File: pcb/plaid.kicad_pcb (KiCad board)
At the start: 2 copper layers, 228 x 98 mm, 134 parts, among them J2 AVR_ISP_6, J3 Conn_01x04, SW1 SW_Push, SW10 SW_Push, SW11 SW_Push, SW12 SW_Push, SW13 SW_Push, SW14 SW_Push, SW15 SW_Push, SW16 SW_Push, SW17 SW_Push, SW18 SW_Push, SW19 SW_Push, SW2 SW_Push, SW20 SW_Push, SW21 SW_Push, SW22 SW_Push, SW23 SW_Push, SW24 SW_Push, SW25 SW_Push, SW26 SW_Push, SW27 SW_Push, SW28 SW_Push, SW29 SW_Push, SW3 SW_Push, SW30 SW_Push, SW31 SW_Push, SW32 SW_Push, SW33 SW_Push, SW34 SW_Push, SW35 SW_Push, SW36 SW_Push, SW37 SW_Push, SW38 SW_Push, SW39 SW_Push, SW4 SW_Push, SW40 SW_Push, SW41 SW_Push, SW42 SW_Push, SW43 SW_Push, SW44 SW_Push, SW45 SW_Push, SW46 SW_Push, SW47 SW_Push, SW48 SW_Push, SW49 SW_Push, SW5 SW_Push, SW50 RESET, SW51 BOOT, SW6 SW_Push, SW7 SW_Push, SW8 SW_Push, SW9 SW_Push, U1 ATMEGA328-PU, Y1 16MHz

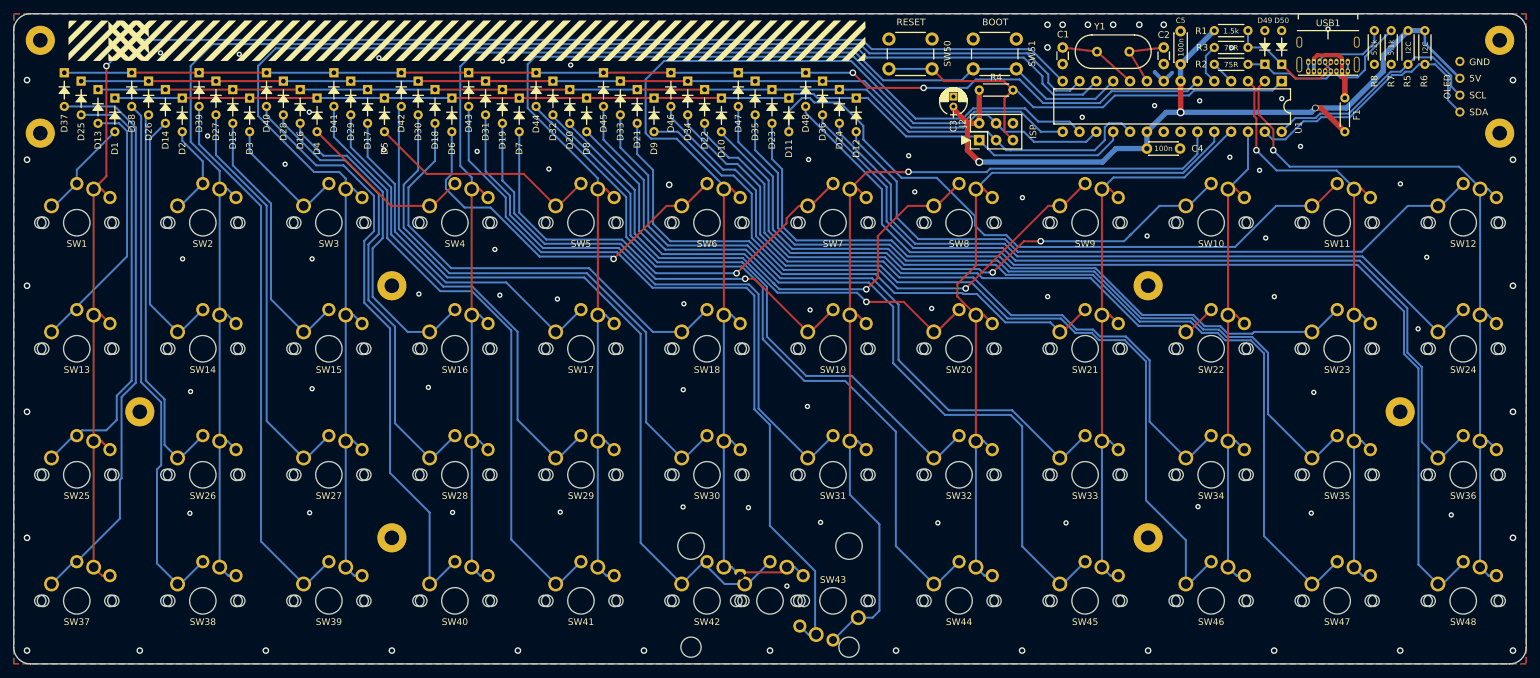
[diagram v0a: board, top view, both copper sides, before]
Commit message: Fix spacebar(s) - use "opposing" footprints
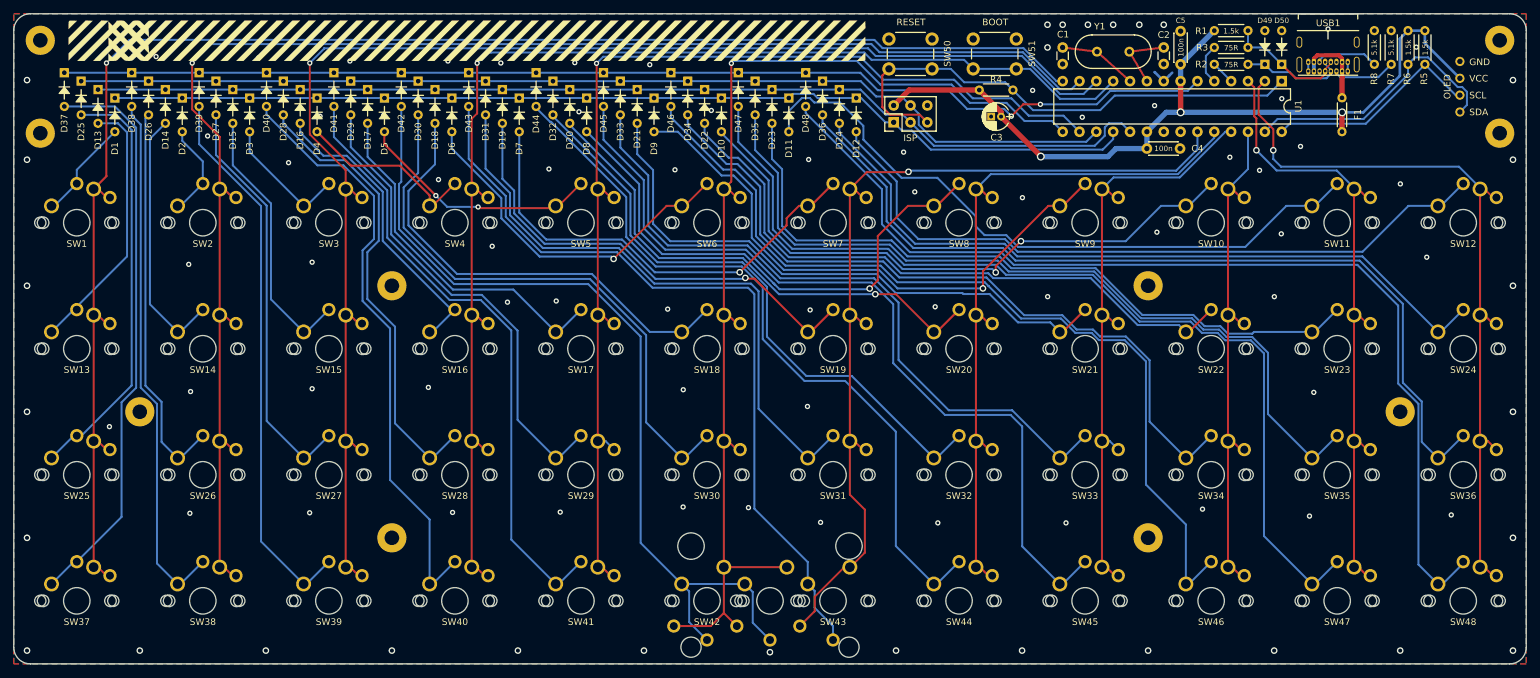
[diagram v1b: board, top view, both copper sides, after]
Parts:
- R5, R6: value I2C -> 1.5k
- SW42, SW43: footprint 42keebs:MX-Choc-1U-NoLED -> 42keebs:MX-Choc-1U-NoLED-opposite
- SW49: footprint 42keebs:MX-Choc-2U-ReversedStabilizers-NoLED -> 42keebs:MX-Choc-2U-ReversedStabilizers-opposite-NoLED
- moved J2 13.2 mm to (165.1, 69.1)
- moved C3 7.34 mm to (181.3, 68.2), turned to 180 degrees
- moved R7 5.08 mm to (240.1, 55.3), turned to -90 degrees
- moved R8 5.08 mm to (237.6, 55.3), turned to -90 degrees
- moved R5 2.54 mm to (245.2, 55.3)
- moved R6 2.54 mm to (242.7, 55.3)
- moved F1 0.44 mm to (232.7, 68.0)
- turned SW43 to 0 degrees
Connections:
- SW43 pad 1: /COL6 -> Net-(D43-Pad2)
- SW43 pad 2: Net-(D43-Pad2) -> /COL6
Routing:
- net /COL4: track 181.8 -> 165.9 mm, vias 0 -> 1
- net /COL2: track 227.1 -> 213.4 mm, vias 0 -> 1
- net Net-(D42-Pad2): track 119.8 -> 132.1 mm
- net /RESET: track 71.3 -> 77.5 mm
- net Net-(D16-Pad2): track 50.0 -> 45.3 mm
- net /COL5: track 172.7 -> 168.3 mm, vias 0 -> 1
- net /COL3: track 192.9 -> 188.8 mm, vias 0 -> 1
- net Net-(R7-Pad2): track 12.9 -> 9.64 mm
- net /COL6: track 141.2 -> 137.9 mm
- net Net-(D6-Pad2): track 57.4 -> 54.4 mm
- net /COL7: track 111.7 -> 109.0 mm
- net /i2c_SDA: track 39.6 -> 41.6 mm
- net Net-(R8-Pad2): track 11.5 -> 9.60 mm
- net /i2c_SCL: track 34.8 -> 33.0 mm
- net Net-(D25-Pad2): track 65.8 -> 64.1 mm
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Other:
- board text added: "Plaid-C // Through Hole // 1.2.42D (c) 2019 Takuya Urakawa, Dm9Records.com Modified by piit79 of 42keebs.eu (2022)"
- board text added: "VCC"
- board text removed: "5V"
- board text removed: "Plaid-C // Through Hole // Rev1.2.42D (c) 2019 Takuya Urakawa, Dm9Records.com Modified by piit79 of 42keebs.eu"
